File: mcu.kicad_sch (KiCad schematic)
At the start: 30 parts, among them J1 Conn_01x02_Socket, U3 RP2350A, X1 ABM8-272-T3

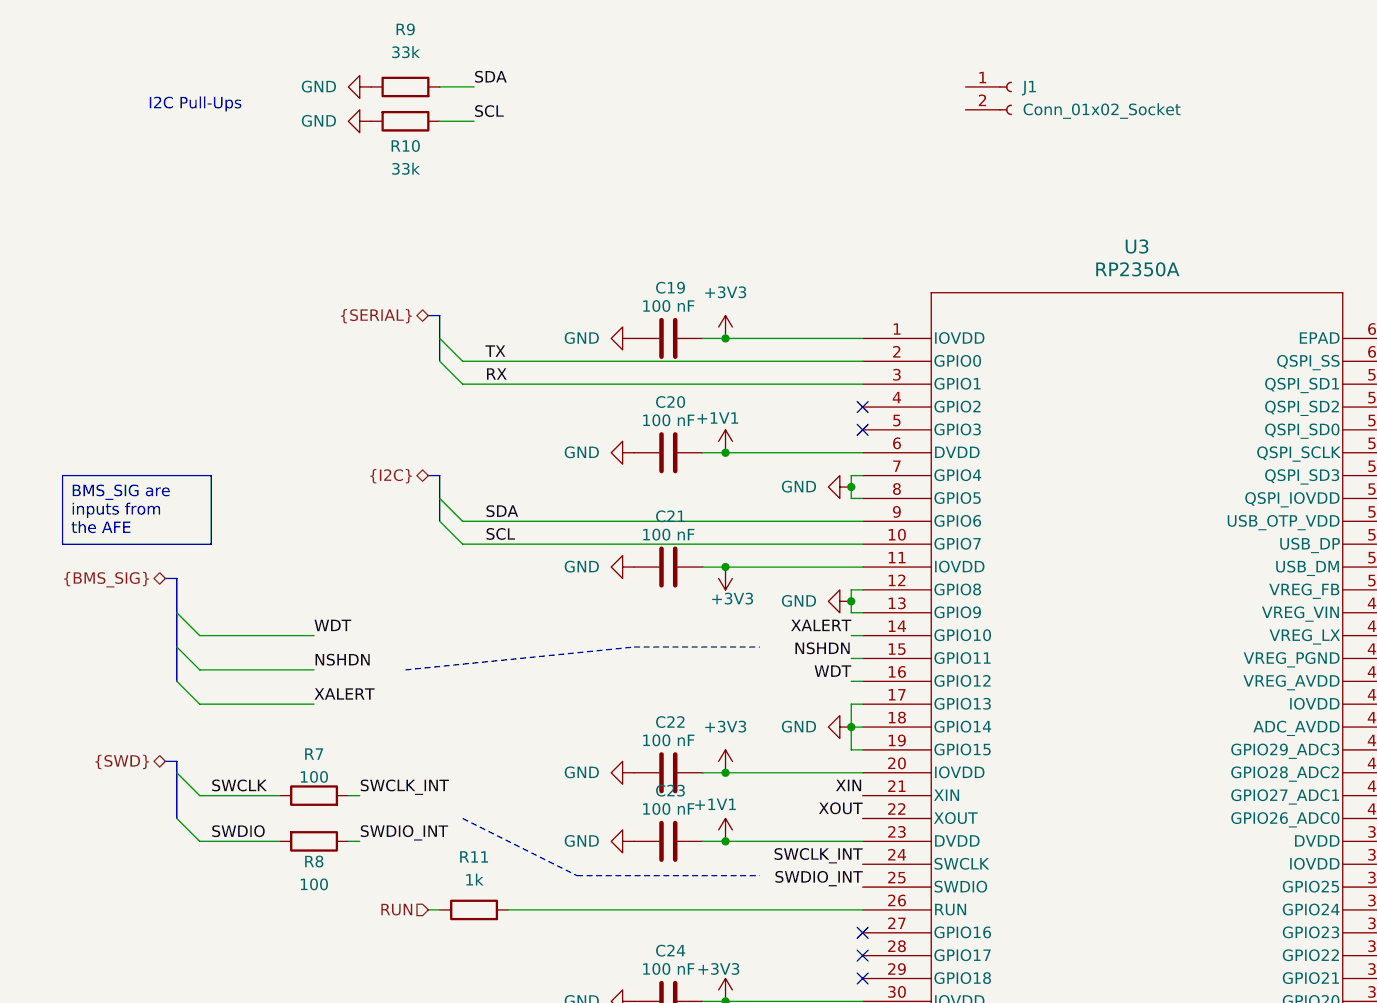
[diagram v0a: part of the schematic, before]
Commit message: Power board prelim routing
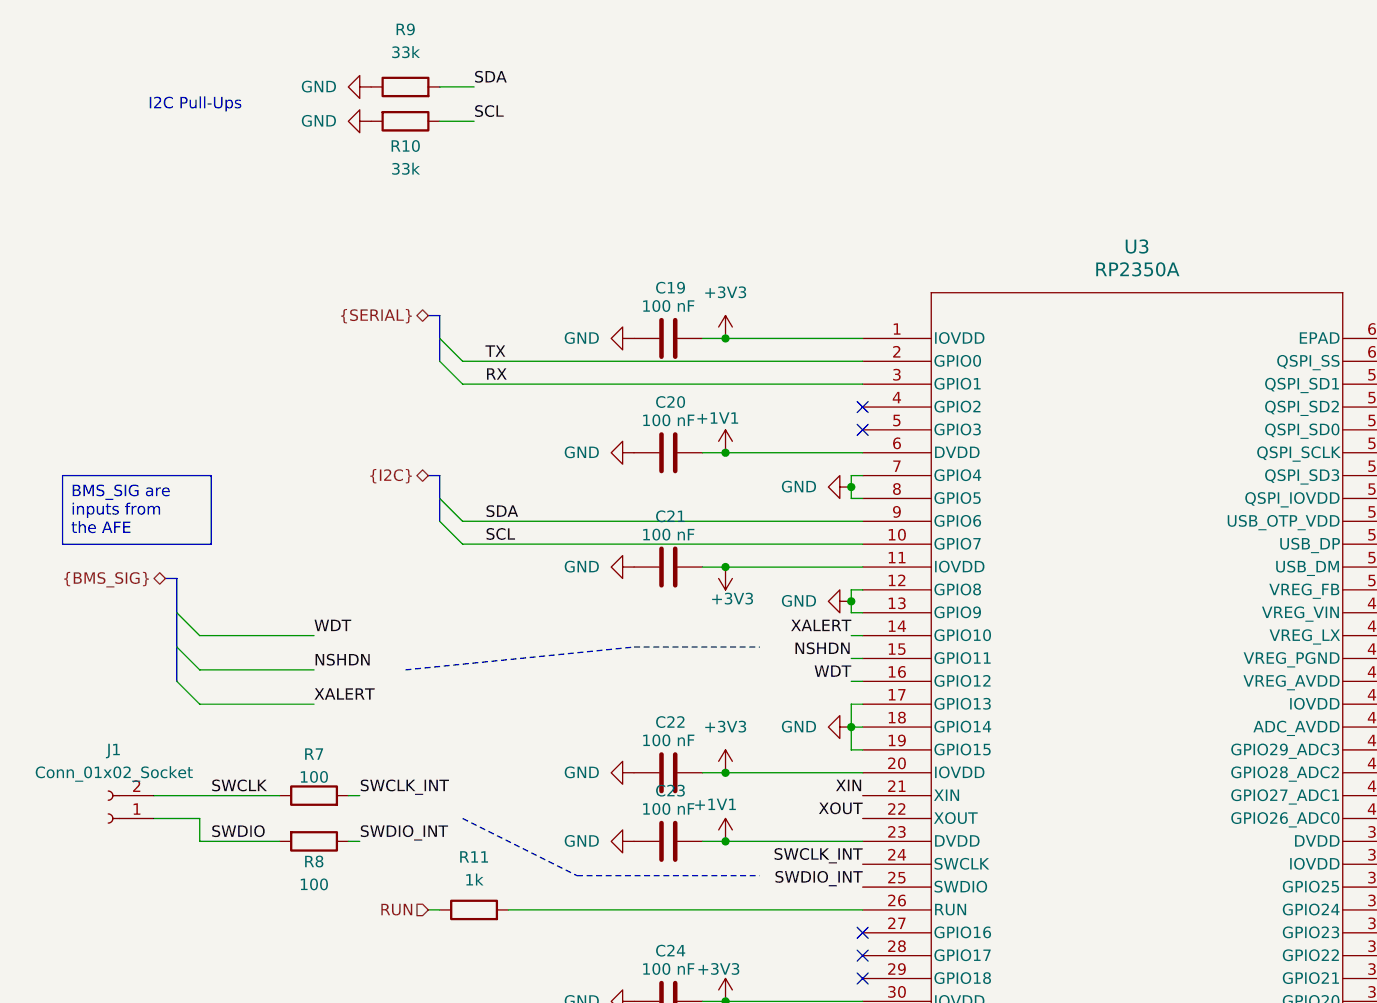
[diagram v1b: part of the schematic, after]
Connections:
- net SWCLK: now also J1.2 (Pin_2)
- net SWDIO: now also J1.1 (Pin_1)
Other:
- moved on the sheet: J1
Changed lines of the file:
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@@
 	)
 	(bus_entry
-		(at 39.37 110.49)
-		(size 2.54 2.54)
-		(stroke
-			(width 0)
-			(type default)
-		)
-	)
-	(bus_entry
 		(at 71.12 80.01)
 		(size -2.54 -2.54)
@@
 		)
 	)
-	(bus_entry
-		(at 39.37 105.41)
-		(size 2.54 2.54)
-		(stroke
-			(width 0)
-			(type default)
-		)
-	)
 	(wire
 		(pts
@@
 		)
 	)
-	(bus
+	(wire
 		(pts
-			(xy 39.37 104.14) (xy 39.37 105.41)
+			(xy 176.53 92.71) (xy 250.19 92.71)
 		)
 		(stroke
@@
 	(wire
 		(pts
-			(xy 176.53 92.71) (xy 250.19 92.71)
+			(xy 41.91 110.49) (xy 41.91 113.03)
 		)
 		(stroke
@@
 		)
 	)
-	(bus
-		(pts
-			(xy 38.1 104.14) (xy 39.37 104.14)
-		)
-		(stroke
-			(width 0)
-			(type default)
-		)
-	)
 	(wire
 		(pts
@@
 		)
 	)
-	(bus
-		(pts
-			(xy 39.37 105.41) (xy 39.37 110.49)
-		)
-		(stroke
-			(width 0)
-			(type default)
-		)
-	)
 	(wire
 		(pts
@@
 	(wire
 		(pts
-			(xy 41.91 107.95) (xy 50.8 107.95)
+			(xy 36.83 107.95) (xy 50.8 107.95)
 		)
 		(stroke
@@
 	(wire
 		(pts
+			(xy 36.83 110.49) (xy 41.91 110.49)
+		)
+		(stroke
+			(width 0)
+			(type default)
+		)
+	)
+	(wire
+		(pts
 			(xy 71.12 62.23) (xy 115.57 62.23)
 		)
@@
 		)
 	)
-	(hierarchical_label "{SWD}"
-		(shape bidirectional)
-		(at 38.1 104.14 180)
-		(effects
-			(font
-				(size 1.27 1.27)
-			)
-			(justify right)
-		)
-	)
 	(hierarchical_label "USB_D+"
 		(shape bidirectional)
@@
 	(symbol
 		(lib_id "Connector:Conn_01x02_Socket")
-		(at 132.08 29.21 0)
+		(at 31.75 110.49 180)
 		(unit 1)
 		(exclude_from_sim no)
@@
 		(fields_autoplaced yes)
 		(property "Reference" "J1"
-			(at 133.35 29.2099 0)
+			(at 32.385 102.87 0)
 			(effects
 				(font
 					(size 1.27 1.27)
 				)
-				(justify left)
 			)
 		)
 		(property "Value" "Conn_01x02_Socket"
-			(at 133.35 31.7499 0)
+			(at 32.385 105.41 0)
 			(effects
 				(font
 					(size 1.27 1.27)
 				)
-				(justify left)
 			)
 		)
 		(property "Footprint" "Connector_JST:JST_PH_B2B-PH-K_1x02_P2.00mm_Vertical"
-			(at 132.08 29.21 0)
+			(at 31.75 110.49 0)
 			(effects
 				(font
@@
 		)
 		(property "Datasheet" "~"
-			(at 132.08 29.21 0)
+			(at 31.75 110.49 0)
 			(effects
 				(font
@@
 		)
 		(property "Description" "Generic connector, single row, 01x02, script generated"
-			(at 132.08 29.21 0)
+			(at 31.75 110.49 0)
 			(effects
 				(font
@@
 		)
 		(property "Mfr" ""
-			(at 132.08 29.21 0)
+			(at 31.75 110.49 0)
 			(effects
 				(font
@@
 		)
 		(property "Mfr P/N" ""
-			(at 132.08 29.21 0)
+			(at 31.75 110.49 0)
 			(effects
 				(font
@@
 		)
 		(property "Supplier_1" ""
-			(at 132.08 29.21 0)
+			(at 31.75 110.49 0)
 			(effects
 				(font
@@
 		)
 		(property "Supplier_1 P/N" ""
-			(at 132.08 29.21 0)
+			(at 31.75 110.49 0)
 			(effects
 				(font
@@
 		)
 		(property "Supplier_1 Unit Price" ""
-			(at 132.08 29.21 0)
+			(at 31.75 110.49 0)
 			(effects
 				(font
@@
 		)
 		(property "Supplier_1 Price @ Qty" ""
-			(at 132.08 29.21 0)
+			(at 31.75 110.49 0)
 			(effects
 				(font
@@
 		)
 		(property "Supplier_2" ""
-			(at 132.08 29.21 0)
+			(at 31.75 110.49 0)
 			(effects
 				(font
@@
 		)
 		(property "Supplier_2 P/N" ""
-			(at 132.08 29.21 0)
+			(at 31.75 110.49 0)
 			(effects
 				(font
@@
 		)
 		(property "Supplier_2 Unit Price" ""
-			(at 132.08 29.21 0)
+			(at 31.75 110.49 0)
 			(effects
 				(font
@@
 		)
 		(property "Supplier_2 Price @ Qty" ""
-			(at 132.08 29.21 0)
+			(at 31.75 110.49 0)
 			(effects
 				(font

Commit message: mcu flash v1
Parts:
- added R74: 10k, Thick Film Resistors - SMD General Purpose Chip Resistor 0603, 10kOhms, 1%, 1/10W, symbol Device:R
- added U17: W25Q128JVS, Package_SO:SOIC-8_5.3x5.3mm_P1.27mm, symbol Memory_Flash:W25Q128JVS
- R10, R9: value 33k -> 10k; footprint Resistor_SMD:R_0603_1608Metric -> Thick Film Resistors - SMD General Purpose Chip Resistor 0603, 10kOhms, 1%, 1/10W; Mfr KOA Speer Electronics, Inc. -> YAGEO; Mfr P/N RN73R1ETTP3302B25 -> RC0603FR-0710KL; Supplier_1 Digikey -> Mouser; Supplier_1 P/N 2019-RN73R1ETTP3302B25TR-ND -> 603-RC0603FR-0710KL
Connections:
- net +3V3: now also R10.2, R9.2, R74.2, U17.8 (VCC); no longer U3.53 (USB_OTP_VDD), U3.54 (QSPI_IOVDD)
- net GND: now also U17.4 (GND); no longer R10.2, R9.1, U3.12 (GPIO8), U3.13 (GPIO9), U3.17 (GPIO13), U3.18 (GPIO14), U3.19 (GPIO15), U3.7 (GPIO4), U3.8 (GPIO5)
- net QSPI_SS: now also R10.1, U17.1 (~{CS})
- net SCL: now also R9.1; no longer R10.1
- net SDA: now also R74.1; no longer R9.2
- net at U3.55 (QSPI_SD3): now also U17.7 (~{HOLD}/~{RESET}/IO_{3})
- net at U3.56 (QSPI_SCLK): now also U17.6 (CLK)
- net at U3.57 (QSPI_SD0): now also U17.5 (DI/IO_{0})
- net at U3.58 (QSPI_SD2): now also U17.3 (~{WP}/IO_{2})
- net at U3.59 (QSPI_SD1): now also U17.2 (DO/IO_{1})
- new net: U3.53 (USB_OTP_VDD), U3.54 (QSPI_IOVDD)
- no-connect marks 21 -> 23
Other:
- moved on the sheet: C29, R9

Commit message: Working on schematic and layout
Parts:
- R10: renamed from R74; footprint Thick Film Resistors - SMD General Purpose Chip Resistor 0603, 10kOhms, 1%, 1/10W -> Resistor_SMD:R_0603_1608Metric
- R12: renamed from R10; footprint Thick Film Resistors - SMD General Purpose Chip Resistor 0603, 10kOhms, 1%, 1/10W -> Resistor_SMD:R_0603_1608Metric
- R9: footprint Thick Film Resistors - SMD General Purpose Chip Resistor 0603, 10kOhms, 1%, 1/10W -> Resistor_SMD:R_0603_1608Metric
- renumbered C19 to C20, C20 to C21, C21 to C22, C22 to C23, C23 to C24, C24 to C25, C25 to C26, C26 to C27, C27 to C28, C28 to C29, C29 to C30, C30 to C31, C31 to C32, C32 to C33, C33 to C34, C34 to C35, R12 to R13, R13 to R14, R14 to R15, R15 to R16, R16 to R17, U17 to U4
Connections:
- net +3V3: now also U3.53 (USB_OTP_VDD), U3.54 (QSPI_IOVDD)
- net BOOT: now also R12.1, R14.1; no longer R14.2
- net QSPI_SS: now also R14.2; no longer R12.1, R14.1
- net QSPI_SD1: now reaches U3.59 (QSPI_SD1), U4.2 (DO/IO_{1})
- net QSPI_SD2: now reaches U3.58 (QSPI_SD2), U4.3 (~{WP}/IO_{2})
- net QSPI_SD0: now reaches U3.57 (QSPI_SD0), U4.5 (DI/IO_{0})
- net QSPI_SCLK: now reaches U3.56 (QSPI_SCLK), U4.6 (CLK)
- net QSPI_SD3: now reaches U3.55 (QSPI_SD3), U4.7 (~{HOLD}/~{RESET}/IO_{3})
- net BATT1.FLTn: now reaches U3.12 (GPIO8)
- net BATT2.FLTn: now reaches U3.13 (GPIO9)
- net BATT2.EN: now reaches U3.17 (GPIO13)
- net NAV1.nFLT: now reaches U3.18 (GPIO14)
- net NAV2.nFLT: now reaches U3.19 (GPIO15)
- net NAV1.nSHDN: now reaches U3.27 (GPIO16)
- net NAV2.nSHDN: now reaches U3.28 (GPIO17)
- net SY_BOOST.PGOOD: now reaches U3.31 (GPIO19)
- net SX_BOOST.PGOOD: now reaches U3.32 (GPIO20)
- net SY_BOOST.EN: now reaches U3.33 (GPIO21)
- net SX_BOOST.EN: now reaches U3.34 (GPIO22)
- net BATT1.PGOOD: now reaches U3.4 (GPIO2)
- net BATT2.IMON: now reaches U3.40 (GPIO26_ADC0)
- net BATT2.IMON: now also U3.41 (GPIO27_ADC1)
- net NAV2.IMON: now reaches U3.42 (GPIO28_ADC2)
- net NAV1.IMON: now reaches U3.43 (GPIO29_ADC3)
- net BATT2.PGOOD: now reaches U3.5 (GPIO3)
- net BATT1.SWEN: now reaches U3.7 (GPIO4)
- net BATT2.SWEN: now reaches U3.8 (GPIO5)
- net NSHDN renamed BATT2.EN_DIODE
- net WDT renamed BATT1.EN
- net XALERT renamed BATT1.EN_DIODE
- no-connect marks 23 -> 6
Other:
- note removed: "EPAD Stitching"
- moved on the sheet: C20, C21, C22, C23, C24, C25, C26, C27, C28, C29, C30, C31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

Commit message: Working on layout
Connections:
- net BATT1.EN: now also U3.13 (GPIO9)
- net BATT1.EN_DIODE: no longer U3.14 (GPIO10)
- net BATT1.IMON: now also U3.41 (GPIO27_ADC1)
- net BATT2.FLTn: no longer U3.13 (GPIO9)
- net BATT2.IMON: no longer U3.41 (GPIO27_ADC1)
- net BATT2.SWEN: now also U3.14 (GPIO10)
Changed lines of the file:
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@@
 		)
 	)
-	(label "BATT2.IMON"
+	(label "BATT1.IMON"
 		(at 232.41 152.4 0)
 		(effects
@@
 		)
 	)
-	(label "BATT2.FLTn"
+	(label "BATT1.EN"
 		(at 171.45 132.08 180)
 		(effects
@@
 		)
 	)
-	(label "BATT1.EN_DIODE"
+	(label "BATT2.SWEN"
 		(at 171.45 134.62 180)
 		(effects

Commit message: Pushing
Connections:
- net B_SENSE_ALERT: now reaches U3.35 (GPIO23)
- net A_SENSE_ALERT: now reaches U3.36 (GPIO24)
- no-connect marks 6 -> 3
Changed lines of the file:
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@@
-	)
-	(no_connect
-		(at 232.41 162.56)
-	)
-	(no_connect
-		(at 232.41 167.64)
 	)
 	(no_connect
@@
 	)
 	(no_connect
-		(at 232.41 165.1)
-	)
-	(no_connect
 		(at 54.61 138.43)
 	)
@@
 	(wire
 		(pts
-			(xy 232.41 160.02) (xy 234.95 160.02)
+			(xy 232.41 160.02) (xy 236.22 160.02)
 		)
 		(stroke
@@
 		(pts
 			(xy 44.45 115.57) (xy 54.61 115.57)
+		)
+		(stroke
+			(width 0)
+			(type default)
+		)
+	)
+	(wire
+		(pts
+			(xy 38.1 204.47) (xy 53.34 204.47)
 		)
 		(stroke
@@
 	(wire
 		(pts
+			(xy 38.1 200.66) (xy 53.34 200.66)
+		)
+		(stroke
+			(width 0)
+			(type default)
+		)
+	)
+	(wire
+		(pts
 			(xy 224.79 212.09) (xy 224.79 210.82)
 		)
@@
 	(wire
 		(pts
-			(xy 250.19 175.26) (xy 252.73 175.26)
+			(xy 251.46 175.26) (xy 252.73 175.26)
 		)
 		(stroke
@@
 	(wire
 		(pts
-			(xy 234.95 160.02) (xy 250.19 175.26)
+			(xy 236.22 160.02) (xy 251.46 175.26)
 		)
 		(stroke
@@
 		)
 	)
+	(label "A_SNS"
+		(at 53.34 200.66 0)
+		(effects
+			(font
+				(size 1.27 1.27)
+			)
+			(justify left bottom)
+		)
+	)
 	(label "SWCLK_INT"
 		(at 171.45 160.02 180)
@@
 		)
 	)
+	(label "B_SNS"
+		(at 53.34 204.47 0)
+		(effects
+			(font
+				(size 1.27 1.27)
+			)
+			(justify left bottom)
+		)
+	)
 	(label "D-"
 		(at 270.51 123.19 0)
@@
 		)
 	)
+	(label "B_SNS"
+		(at 232.41 167.64 0)
+		(effects
+			(font
+				(size 1.27 1.27)
+			)
+			(justify left bottom)
+		)
+	)
 	(label "BATT1.IMON"
 		(at 54.61 113.03 0)
@@
 	(label "SY_BOOST.EN"
 		(at 232.41 172.72 0)
+		(effects
+			(font
+				(size 1.27 1.27)
+			)
+			(justify left bottom)
+		)
+	)
+	(label "A_SNS"
+		(at 232.41 165.1 0)
 		(effects
 			(font
@@
 		)
 	)
+	(hierarchical_label "A_SENSE_ALERT"
+		(shape input)
+		(at 38.1 200.66 180)
+		(effects
+			(font
+				(size 1.27 1.27)
+			)
+			(justify right)
+		)
+	)
 	(hierarchical_label "SY_BOOST{SIG_BOOST}"
 		(shape bidirectional)
@@
 		(effects
 			(font
+				(size 1.27 1.27)
+			)
+			(justify right)
+		)
+	)
+	(hierarchical_label "B_SENSE_ALERT"
+		(shape input)
+		(at 38.1 204.47 180)
+		(effects
+			(font

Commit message: home stretch
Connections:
- net BATT1.EN: no longer U3.13 (GPIO9)
- net BATT1.EN_DIODE: now also U3.14 (GPIO10)
- net BATT2.SWEN: no longer U3.14 (GPIO10)
- no-connect marks 3 -> 4
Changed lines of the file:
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@@
 	)
 	(no_connect
+		(at 171.45 132.08)
+	)
+	(no_connect
 		(at 54.61 118.11)
 	)
@@
 	(wire
 		(pts
+			(xy 142.24 175.26) (xy 146.05 175.26)
+		)
+		(stroke
+			(width 0)
+			(type default)
+		)
+	)
+	(wire
+		(pts
 			(xy 44.45 190.5) (xy 53.34 190.5)
 		)
@@
 		)
 	)
-	(label "BATT1.EN"
-		(at 171.45 132.08 180)
-		(effects
-			(font
-				(size 1.27 1.27)
-			)
-			(justify right bottom)
-		)
-	)
 	(label "NAV1.nSHDN"
 		(at 171.45 167.64 180)
@@
 		)
 	)
-	(label "BATT2.SWEN"
-		(at 171.45 134.62 180)
-		(effects
-			(font
-				(size 1.27 1.27)
-			)
-			(justify right bottom)
-		)
-	)
 	(label "BATT1.EN"
 		(at 54.61 123.19 0)
@@
 		)
 	)
+	(label "BATT1.EN_DIODE"
+		(at 171.45 134.62 180)
+		(effects
+			(font
+				(size 1.27 1.27)
+			)
+			(justify right bottom)
+		)
+	)
 	(label "BATT1.SWEN"
 		(at 54.61 120.65 0)
@@
 		(dnp no)
 		(property "Reference" "C25"
-			(at 150.114 169.672 90)
+			(at 146.304 169.672 90)
 			(effects
 				(font
@@
 		)
 		(property "Value" "100 nF"
-			(at 149.86 171.704 90)
+			(at 146.05 171.704 90)
 			(effects
 				(font
@@
 	(symbol
 		(lib_id "power:GND")
-		(at 146.05 175.26 270)
+		(at 142.24 175.26 270)
 		(unit 1)
 		(exclude_from_sim no)
@@
 		(fields_autoplaced yes)
 		(property "Reference" "#PWR027"
-			(at 139.7 175.26 0)
+			(at 135.89 175.26 0)
 			(effects
 				(font
@@
 		)
 		(property "Value" "GND"
-			(at 142.24 175.2599 90)
+			(at 138.43 175.2599 90)
 			(effects
 				(font
@@
 		)
 		(property "Footprint" ""
-			(at 146.05 175.26 0)
+			(at 142.24 175.26 0)
 			(effects
 				(font
@@
 		)
 		(property "Datasheet" ""
-			(at 146.05 175.26 0)
+			(at 142.24 175.26 0)
 			(effects
 				(font
@@
 		)
 		(property "Description" "Power symbol creates a global label with name \"GND\" , ground"
-			(at 146.05 175.26 0)
+			(at 142.24 175.26 0)
 			(effects
 				(font

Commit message: home stretch (sike)
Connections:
- net BATT2.PGOOD: now also U3.29 (GPIO18); no longer U3.5 (GPIO3)
- net SY_BOOST.EN: now also U3.5 (GPIO3); no longer U3.33 (GPIO21)
- no-connect marks 4 -> 5

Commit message: BOM in folder
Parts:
- C20, C21, C22, C23, C24, C25, C28, C29, C30, C32: JLCPCB Status (none) -> JLC in-stock package match; Mfr P/N GRM155C71H104JE19D -> CC0603KRX7R9BB104; Supplier_1 DigiKey -> LCSC; Supplier_1 P/N 490-GRM155C71H104JE19DTR-ND -> C14663; Supplier_1 Unit Price 0.10000 -> (none)
- C26, C27: JLCPCB Status (none) -> JLC in-stock package match; Mfr P/N GRM0335C1E150JA01D -> CC0603JRNPO9BN150; Supplier_1 Digikey -> LCSC; Supplier_1 P/N 490-9658-2-ND -> C107037; Supplier_1 Unit Price 0.10000 -> (none)
- C31, C33, C34, C35: JLCPCB Status (none) -> JLC in-stock package match; Mfr P/N GRM155R60J475ME87D -> CL10A475KO8NNNC; Supplier_1 Digkey -> LCSC; Supplier_1 P/N 490-5408-2-ND -> C19666; Supplier_1 Unit Price 0.10000 -> (none)
- J1: Supplier_1 (none) -> LCSC; Supplier_1 P/N (none) -> C173752
- L2: JLCPCB Status (none) -> Similar JLC in-stock package match; Mfr P/N AOTA-B201610S3R3-101-T -> LQM21PN3R3MGRD; Supplier_1 Digikey -> LCSC; Supplier_1 P/N 535-AOTA-B201610S3R3-101-TTR-ND -> C162585; Supplier_1 Unit Price 0.22000 -> (none)
- R10, R12, R9: JLCPCB Status (none) -> JLC in-stock package match; Mfr P/N RC0603FR-0710KL -> 0603WAF1002T5E; Supplier_1 Mouser -> LCSC; Supplier_1 P/N 603-RC0603FR-0710KL -> C25804; Supplier_1 Unit Price 0.10000 -> (none)
- R11, R14: JLCPCB Status (none) -> JLC in-stock package match; Mfr P/N RK73H1ERTTP1001F -> 0603WAF1001T5E; Supplier_1 Digikey -> LCSC; Supplier_1 P/N 2019-RK73H1ERTTP1001FTR-ND -> C21190; Supplier_1 Unit Price 0.13000 -> (none)
- R13: JLCPCB Status (none) -> JLC in-stock package match; Mfr P/N CR0201AFW-1001GAS -> 0603WAF1001T5E; Supplier_1 Digikey -> LCSC; Supplier_1 P/N CR0201AFW-1001GASTR-ND -> C21190; Supplier_1 Unit Price 0.1 -> (none)
- R15, R16: JLCPCB Status (none) -> Similar JLC in-stock package match; Mfr P/N RC0201FR-0727RL -> FRC0603F27R0TS; Supplier_1 Digikey -> LCSC; Supplier_1 P/N YAG2554TR-ND -> C2907021; Supplier_1 Unit Price 0.10000 -> (none)
- R17: JLCPCB Status (none) -> Similar JLC in-stock package match; Mfr P/N TNPW040233R0DEED -> FRC0603F33R0TS; Supplier_1 Digikey -> LCSC; Supplier_1 P/N 541-TNPW040233R0DEEDTR-ND -> C2909394; Supplier_1 Unit Price 0.20000 -> (none)
- R7, R8: JLCPCB Status (none) -> JLC in-stock package match; Mfr P/N AC0201FR-07100RL -> RC0603FR-07100RL; Supplier_1 Digikey -> LCSC; Supplier_1 P/N YAG3412TR-ND -> C105588; Supplier_1 Unit Price 0.10000 -> (none)
- U3: JLCPCB Status (none) -> JLC in-stock package match; Mfr P/N SC1511(13)-A4 -> RP2350A; Supplier_1 Digikey -> LCSC; Supplier_1 P/N 2648-SC1511(13)-A4TR-ND -> C42411118; Supplier_1 Unit Price 1.00000 -> (none)
- U4: JLCPCB Status (none) -> Similar JLC in-stock package match; Mfr P/N (none) -> W25Q128JVSIQ; Supplier_1 (none) -> LCSC; Supplier_1 P/N (none) -> C97521
- X1: Supplier_1 Digikey -> LCSC; Supplier_1 P/N 535-ABM8-272-T3TR-ND -> C20625731; Supplier_1 Unit Price 0.66000 -> (none)
